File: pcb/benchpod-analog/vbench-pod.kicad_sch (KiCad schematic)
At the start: 4 parts

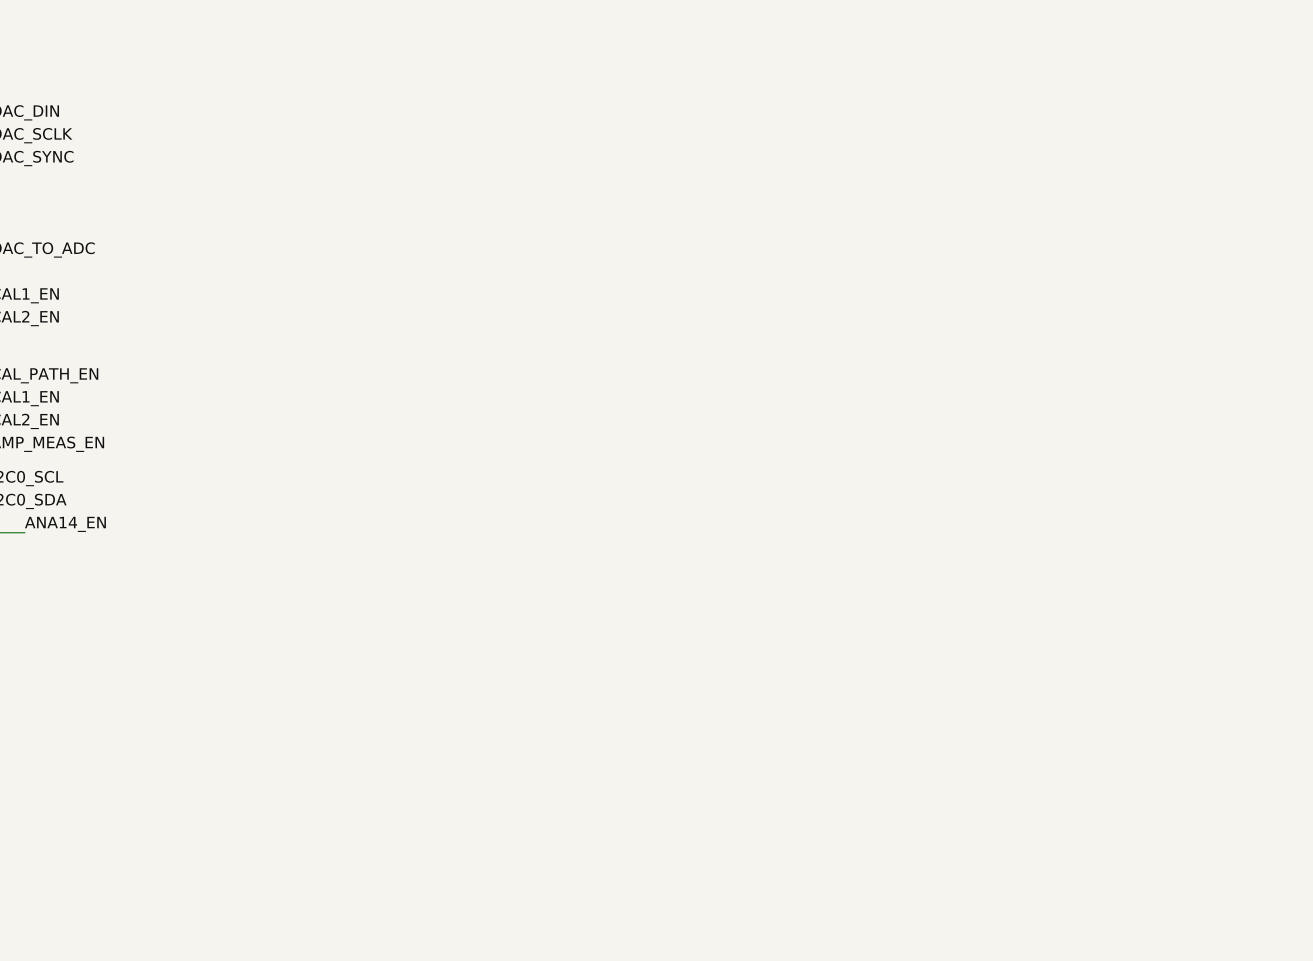
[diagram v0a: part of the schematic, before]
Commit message: analog only board: CN1 FFC module link to the digital board
- CN1 KH-FPC1.0-H2.0SMT-24P-QCHF (C5123103), the same 24-pin 1.0 mm FFC
  connector as the digital board, on the root sheet. Pins 21-24 +5V,
  DAC_DIN/SCLK/SYNC, ADC_SDI/SCLK/SDO/CNVST and I2C0 to the existing labels;
  MOD_PRESENT# tied to GND; MOD_RESET# and MOD_SPARE unused; tabs to GND.
- Placed on the bottom side, under the digital CN1 (same X/Y from the
  top-left board corner), opening toward the left edge. Mounted upside down
  it is mirrored, so the pin order is reversed: pin N here = digital CN1
  pin 25-N (a flat cable keeps each wire at the same position). Text note on
  the sheet.
- PCB: only the footprint was added; it overlaps existing B.Cu routing
  (-14V_ANA, +5V, ANA14_EN, GND vias) that needs rerouting.

Co-Authored-By: Claude Opus 5.5 <noreply@anthropic.com>
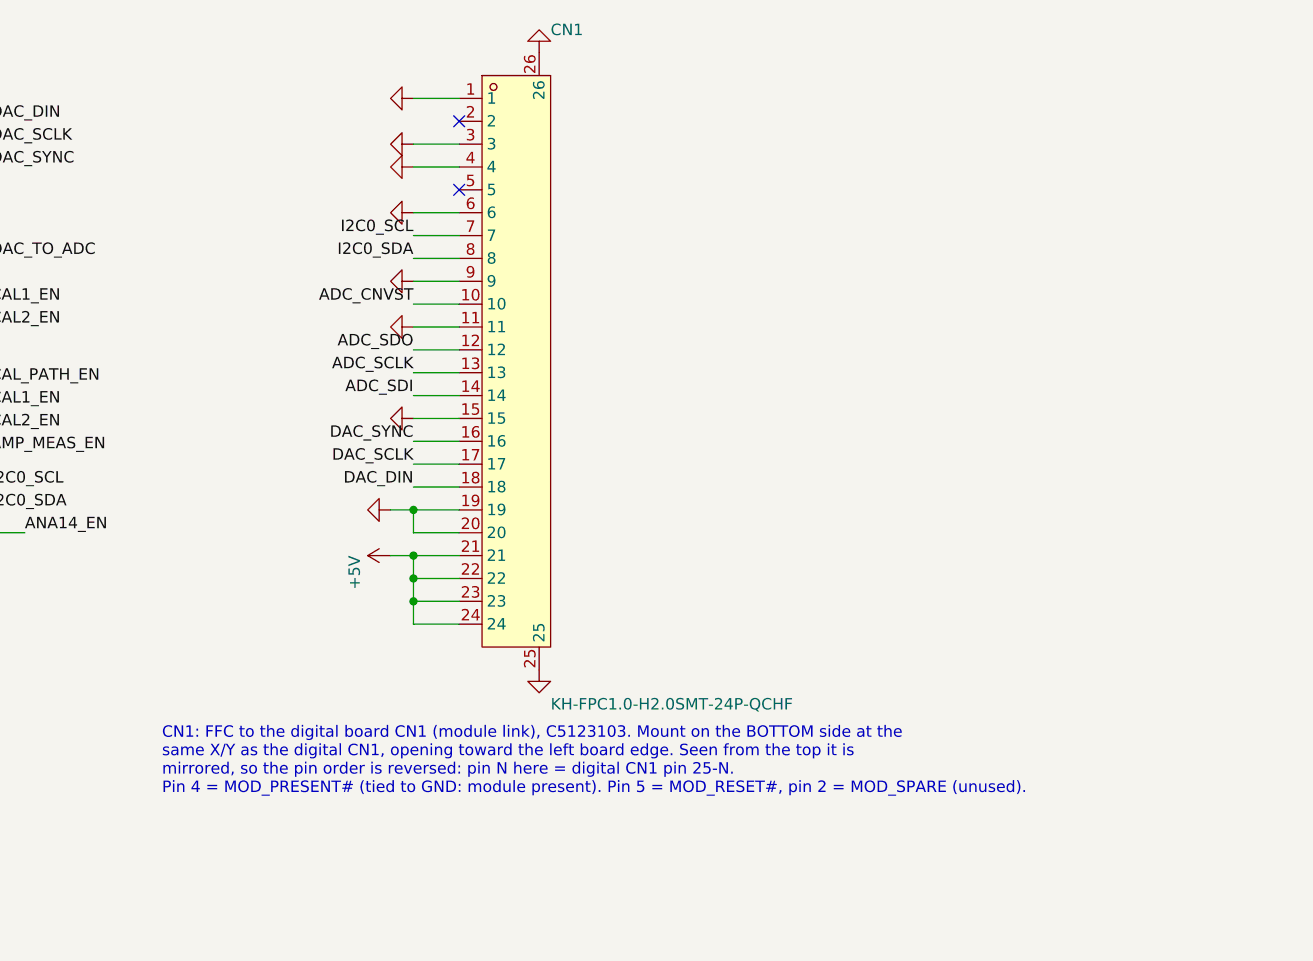
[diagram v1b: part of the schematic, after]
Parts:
- added CN1: KH-FPC1.0-H2.0SMT-24P-QCHF, lcsc_footprints:C5123103_FPC-SMD_24P-P1.00_KH-FPC1.0-H2.0SMT-24P-QCHF, symbol lcsc_imported:KH-FPC1.0-H2.0SMT-24P-QCHF_C5123103
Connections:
- net ADC_CNVST: now also CN1.10
- net ADC_SCLK: now also CN1.13
- net ADC_SDI: now also CN1.14
- net ADC_SDO: now also CN1.12
- net DAC_DIN: now also CN1.18
- net DAC_SCLK: now also CN1.17
- net DAC_SYNC: now also CN1.16
- net GND: now also CN1.1, CN1.11, CN1.15, CN1.19, CN1.20, CN1.25, CN1.26, CN1.3, CN1.4, CN1.6, CN1.9
- net I2C0_SCL: now also CN1.7
- net I2C0_SDA: now also CN1.8
- new net +5V: CN1.21, CN1.22, CN1.23, CN1.24
- no-connect marks 0 -> 2
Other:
- note added: "CN1: FFC to the digital board CN1 (module link), C5123103. Mount on the BOTTOM side at the same X/Y as the digital CN1, opening toward the left board edge. Seen from the top it is mirrored, so the pin order is reversed: pin N here = digital CN1 pin 25-N. Pin 4 = MOD_PRESENT# (tied to GND: module present). Pin 5 = MOD_RESET#, pin 2 = MOD_SPARE (unused)."

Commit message: analog only board: sheet-pin cleanup, PWR_FLAGs, module ID EEPROM
- Power sheet: the INA_SCL/SDA, SCL/SDA and EFUSE_INT sheet pins and their
  root labels removed (left over from the full pod, no labels inside).
- PWR_FLAG on +5V at CN1 (it now comes in over the FFC) and on GND.
- U61 24C32 I2C EEPROM (XBLW 24C32BN, C18723546, SOP-8) on I2C0, the module
  bus: A0-A2 and WP to GND (address 0x50, writable), C268 100n. Holds the
  module ID and its DAC/ADC calibration so they travel with the module.
  Pull-ups are on the digital board (R193/R194).

BOM: +1 line (EEPROM). ERC 291 -> 276 (6 cleanup errors gone).

Co-Authored-By: Claude Opus 5.5 <noreply@anthropic.com>
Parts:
- added C268: 100n, Capacitor_SMD:C_0402_1005Metric, symbol Device:C
- added U61: 24C32, lcsc_footprints:C18723546_SOP-8_L4.9-W3.9-P1.27-LS6.0-BL, symbol Memory_EEPROM:24LC32
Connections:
- net GND: now also C268.2, U61.1 (A0), U61.2 (A1), U61.3 (A2), U61.4 (GND), U61.7 (WP)
- net I2C0_SCL: now also U61.6 (SCL)
- net I2C0_SDA: now also U61.5 (SDA)
- new net +3V3: C268.1, U61.8 (VCC)
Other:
- sheet Power ports: added none; removed EFUSE_INT, INA_SCL, INA_SDA, SCL, SDA
- note added: "U61: module ID + calibration EEPROM (24C32, 0x50). WP = GND (writable). Pull-ups on the digital board."

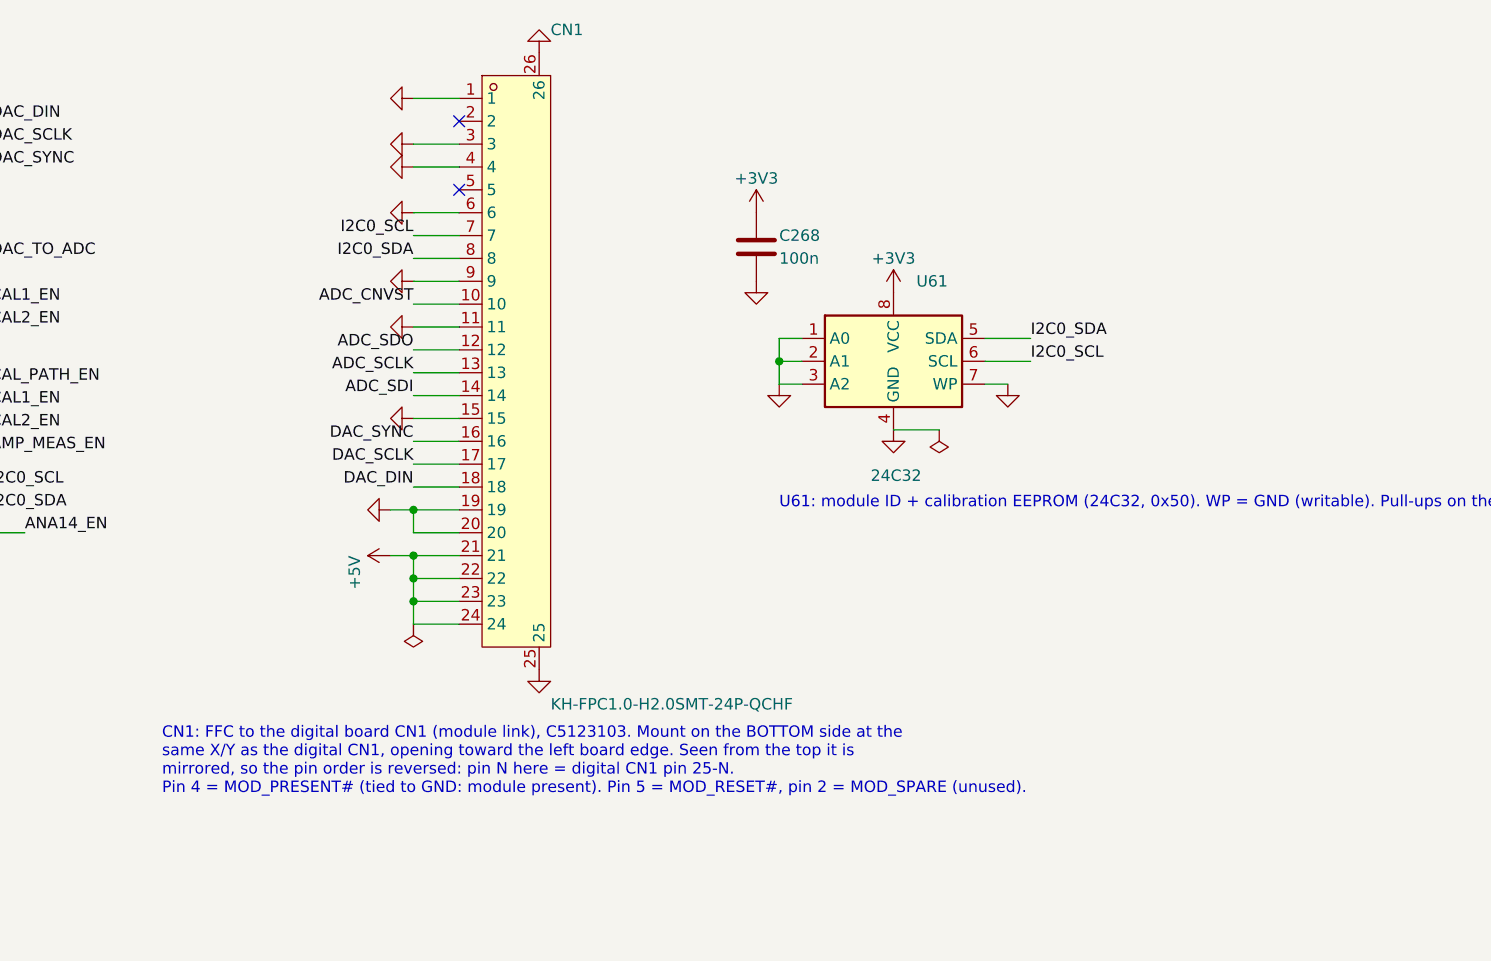
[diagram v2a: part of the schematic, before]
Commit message: analog only board: CN1 on the top side, straight pin order
The board now has a cut at the left edge for the FFC, so CN1 moves to the
top side with the same orientation as the digital CN1 (opening toward the
cut). The cable U-turns through the cut, so pin N = digital CN1 pin N again
(the reversed mapping is gone): pins 1-4 +5V, MOD_PRESENT# (21) to GND,
MOD_RESET# (20) and MOD_SPARE (23) unused. Note on the sheet updated.

PCB: CN1 on F.Cu, rotated -90, pin 1 at the digital pin-1 height (y 48.57
from the top edge), 2 mm further inboard (x 19.51) so the opening is about
3.3 mm from the cut's inner edge and the cable has room to bend.
Includes the board-edge cut drawn in KiCad.

Co-Authored-By: Claude Opus 5.5 <noreply@anthropic.com>
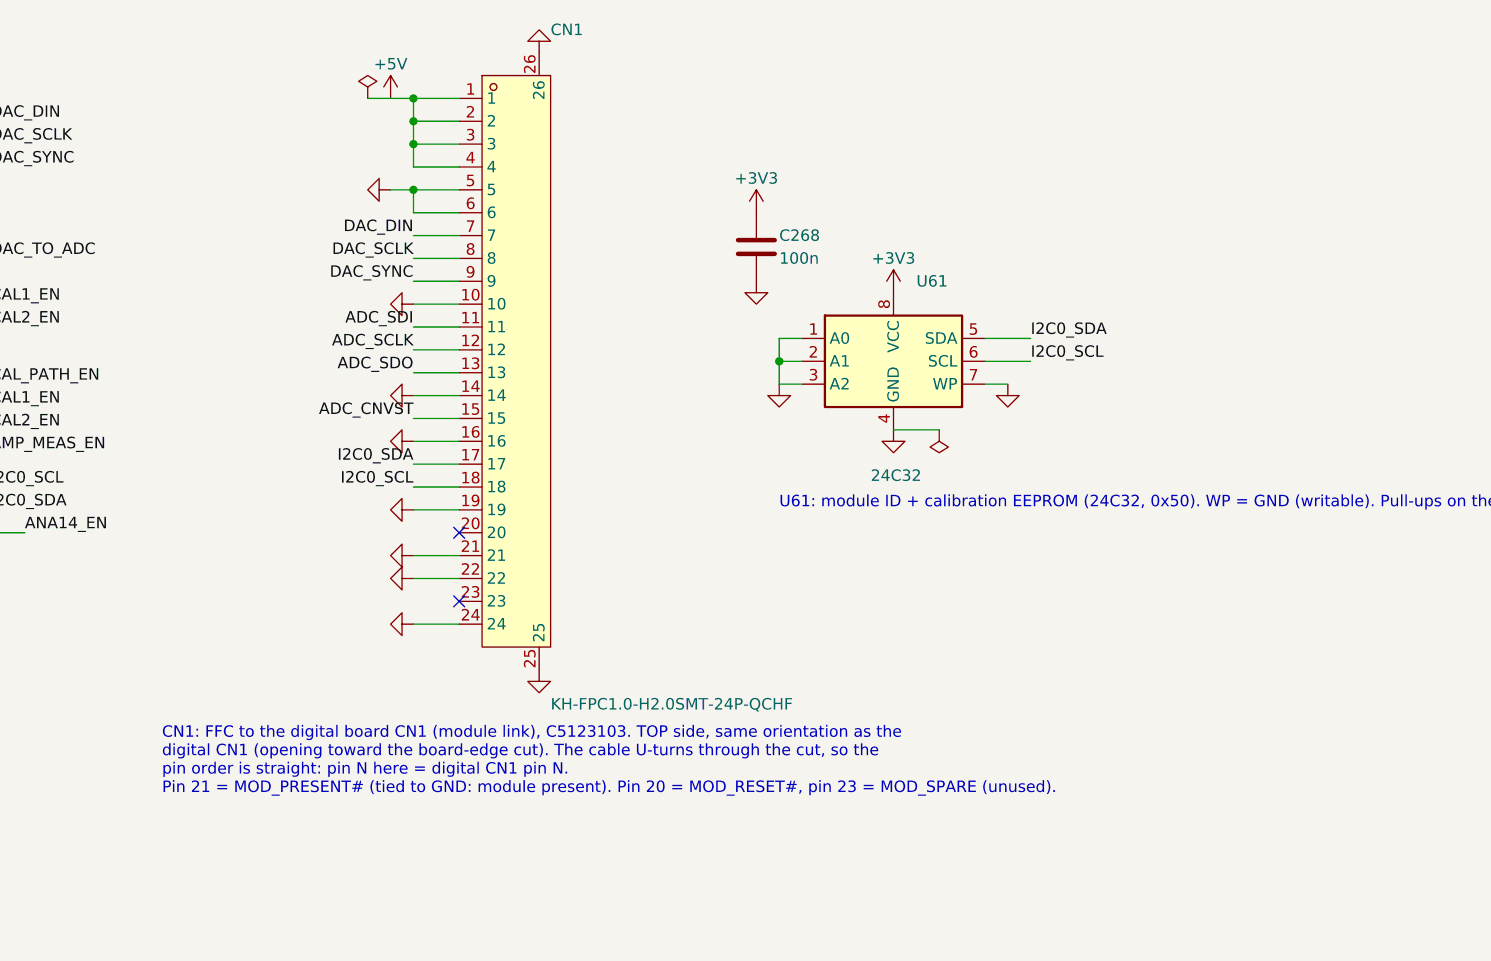
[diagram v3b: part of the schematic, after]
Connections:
- net +5V: now also CN1.1, CN1.2, CN1.3, CN1.4; no longer CN1.21, CN1.22, CN1.23, CN1.24
- net ADC_CNVST: now also CN1.15; no longer CN1.10
- net ADC_SCLK: now also CN1.12; no longer CN1.13
- net ADC_SDI: now also CN1.11; no longer CN1.14
- net ADC_SDO: now also CN1.13; no longer CN1.12
- net DAC_DIN: now also CN1.7; no longer CN1.18
- net DAC_SCLK: now also CN1.8; no longer CN1.17
- net DAC_SYNC: now also CN1.9; no longer CN1.16
- net GND: now also CN1.10, CN1.14, CN1.16, CN1.21, CN1.22, CN1.24, CN1.5; no longer CN1.1, CN1.11, CN1.15, CN1.20, CN1.3, CN1.4, CN1.9
- net I2C0_SCL: now also CN1.18; no longer CN1.7
- net I2C0_SDA: now also CN1.17; no longer CN1.8
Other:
- note added: "CN1: FFC to the digital board CN1 (module link), C5123103. TOP side, same orientation as the digital CN1 (opening toward the board-edge cut). The cable U-turns through the cut, so the pin order is straight: pin N here = digital CN1 pin N. Pin 21 = MOD_PRESENT# (tied to GND: module present). Pin 20 = MOD_RESET#, pin 23 = MOD_SPARE (unused)."
- note removed: "CN1: FFC to the digital board CN1 (module link), C5123103. Mount on the BOTTOM side at the same X/Y as the digital CN1, opening toward the left board edge. Seen from the top it is mirrored, so the pin order is reversed: pin N here = digital CN1 pin 25-N. Pin 4 = MOD_PRESENT# (tied to GND: module present). Pin 5 = MOD_RESET#, pin 2 = MOD_SPARE (unused)."
